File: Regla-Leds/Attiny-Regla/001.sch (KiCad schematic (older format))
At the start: 20 parts, among them J1 CONN_02X03, J2 CONN_01X02, J3 CONN_01X02, SW1 SW_SPDT, U1 ATTINY85-20SU, U2 LM340MP-5.0/NOPB

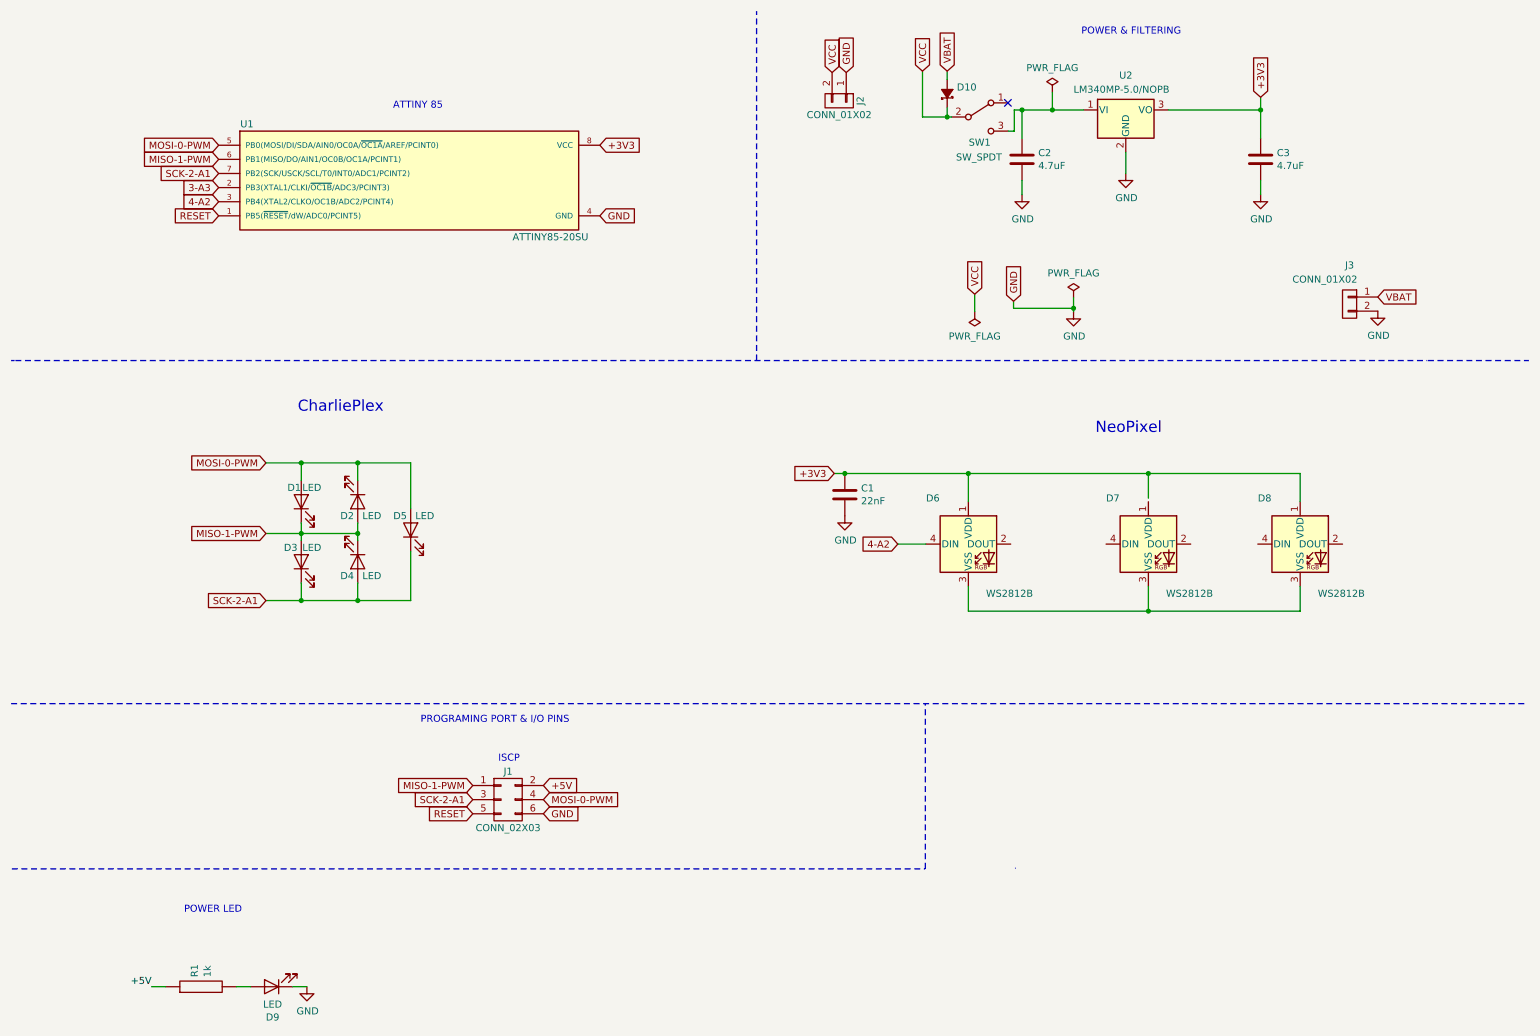
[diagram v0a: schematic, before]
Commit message: Add Moon Reverse Led Kit
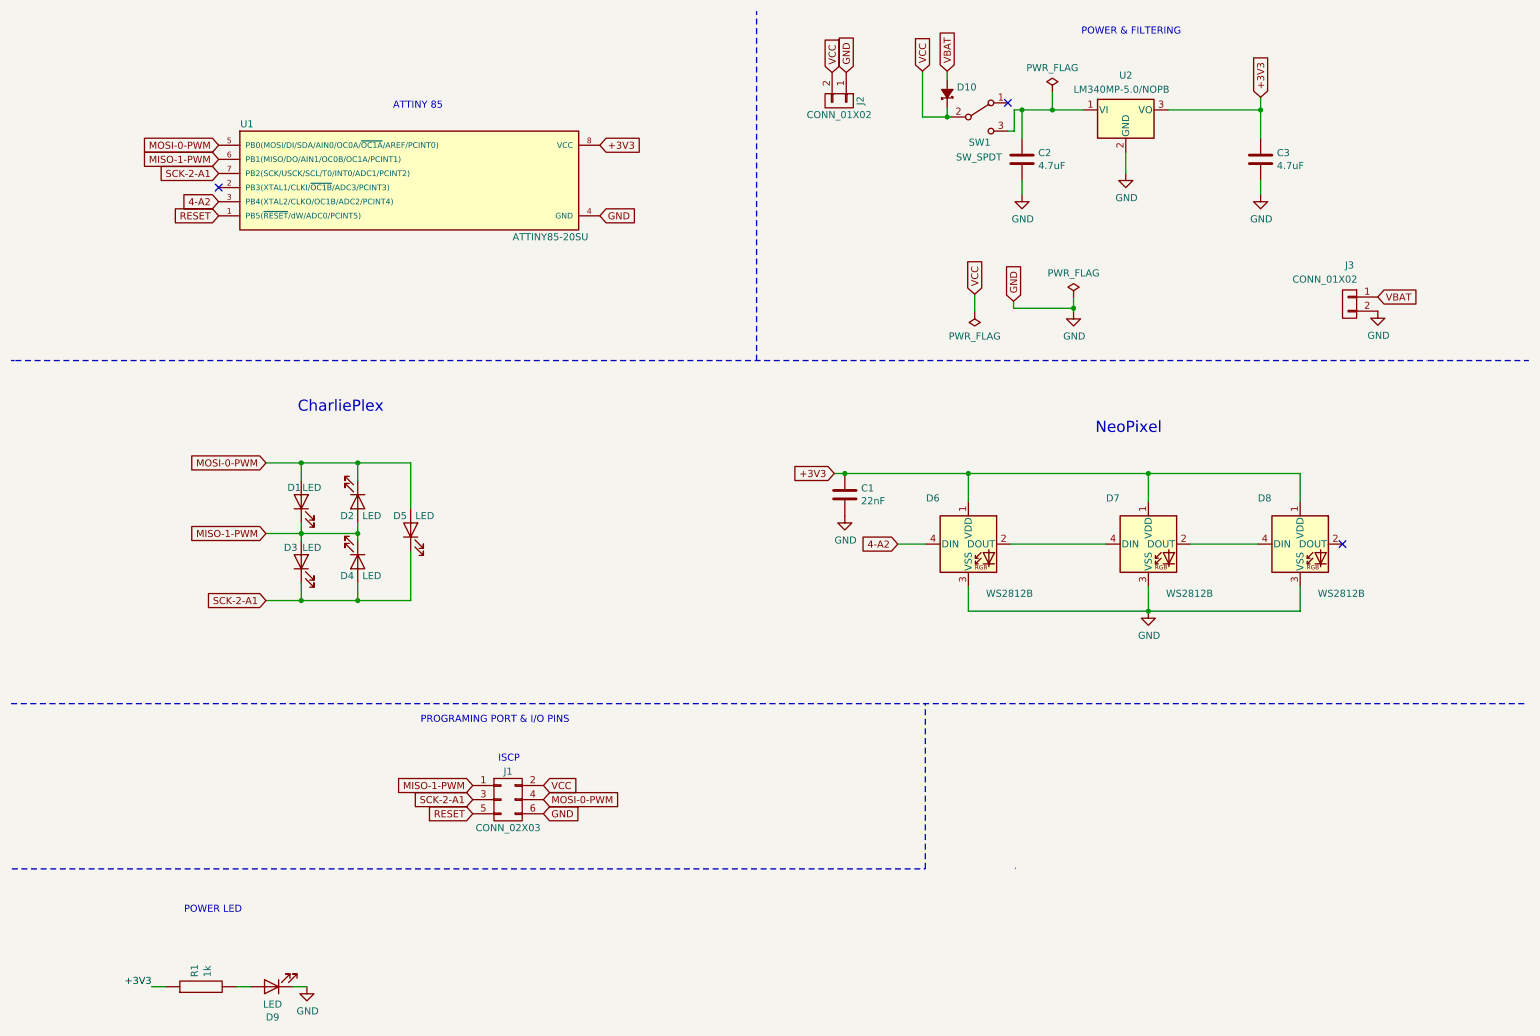
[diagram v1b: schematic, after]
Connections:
- net +3V3: now also D7.1 (VDD), R1.1
- net GND: now also D6.3 (VSS), D7.3 (VSS), D8.3 (VSS)
- net VCC: now also J1.2 (P2)
- net at D6.2 (DOUT): now also D7.4 (DIN)
- net at D7.2 (DOUT): now also D8.4 (DIN)
- removed net +5V: J1.2 (P2), R1.1
- net 3-A3: no longer names the net of U1.2 (PB3(XTAL1/CLKI/~OC1B~/ADC3/PCINT3))
- no-connect marks 1 -> 3
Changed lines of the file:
@@
 $EndComp
 Text Label 1465 7385 2    50   ~ 0
-+5V
++3V3
 $Comp
 L power:GND #PWR02
@@
 	1    0    0    -1
 $EndComp
-Text GLabel 4240 5960 2    50   Input ~ 0
-+5V
 Text GLabel 7100 900  1    50   Input ~ 0
 VBAT
@@
 Text GLabel 1940 1425 0    50   Input ~ 0
 MOSI-0-PWM
-Text GLabel 1940 1725 0    50   Input ~ 0
-3-A3
 Text GLabel 1940 1825 0    50   Input ~ 0
 4-A2
@@
 Wire Wire Line
 	7250 3750 7250 3950
-Wire Wire Line
-	8525 3925 8525 3750
 Connection ~ 8525 3750
 Wire Wire Line
@@
 Text Notes 8150 3475 0    79   ~ 0
 NeoPixel
+Wire Wire Line
+	7550 4250 8225 4250
+Wire Wire Line
+	8825 4250 9300 4250
+Wire Wire Line
+	8525 3750 8525 3950
+NoConn ~ 9900 4250
+$Comp
+L power:GND #PWR08
+U 1 1 5D911307
+P 8525 4725
+F 0 "#PWR08" H 8525 4475 50  0001 C CNN
+F 1 "GND" H 8530 4552 50  0000 C CNN
+F 2 "" H 8525 4725 50  0001 C CNN
+F 3 "" H 8525 4725 50  0001 C CNN
+	1    8525 4725
+	1    0    0    -1
+$EndComp
+Text GLabel 4240 5960 2    50   Input ~ 0
+VCC
+NoConn ~ 1940 1725
 $EndSCHEMATC
